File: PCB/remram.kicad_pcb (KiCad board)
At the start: 4 copper layers, 140 x 103 mm, 208 parts, among them J1 4DB-P108-06, J10 70543-0002, J11 Conn_02x13_Odd_Even, J12 70543-0002, J13 70543-0002, J14 70543-0002, J15 70543-0003, J16 62201021121, J17 70543-0001, J18 70543-0001, J19 70543-0001, J2 039531-1002, J20 70543-0003, J21 70543-0003, J22 70543-0003, J23 70543-0003, J3 70543-0002, J4 70543-0002, J5 70543-0002, J6 67068-8000, J7 Conn_02x05, J8 Conn_02x05, J9 70543-0002, Q1 PSMN1R2-30YLC,115, Q2 BUK9840-55, Q3 PSMN1R2-30YLC,115, Q4 BUK9840-55, SW1 OS102011MA1QN1, SW2 PTS645VL39-2, U1 TPS54308, U2 AP2112K-3.3TRG1, U3 ADUM4160, U4 STM32F765VIT6, U5 TMC2130-TA, U6 TMC2130-TA, U7 TMC2130-TA, U8 TMC2130-TA, Y1 TSX-3225 24.0000MF15X-AC3

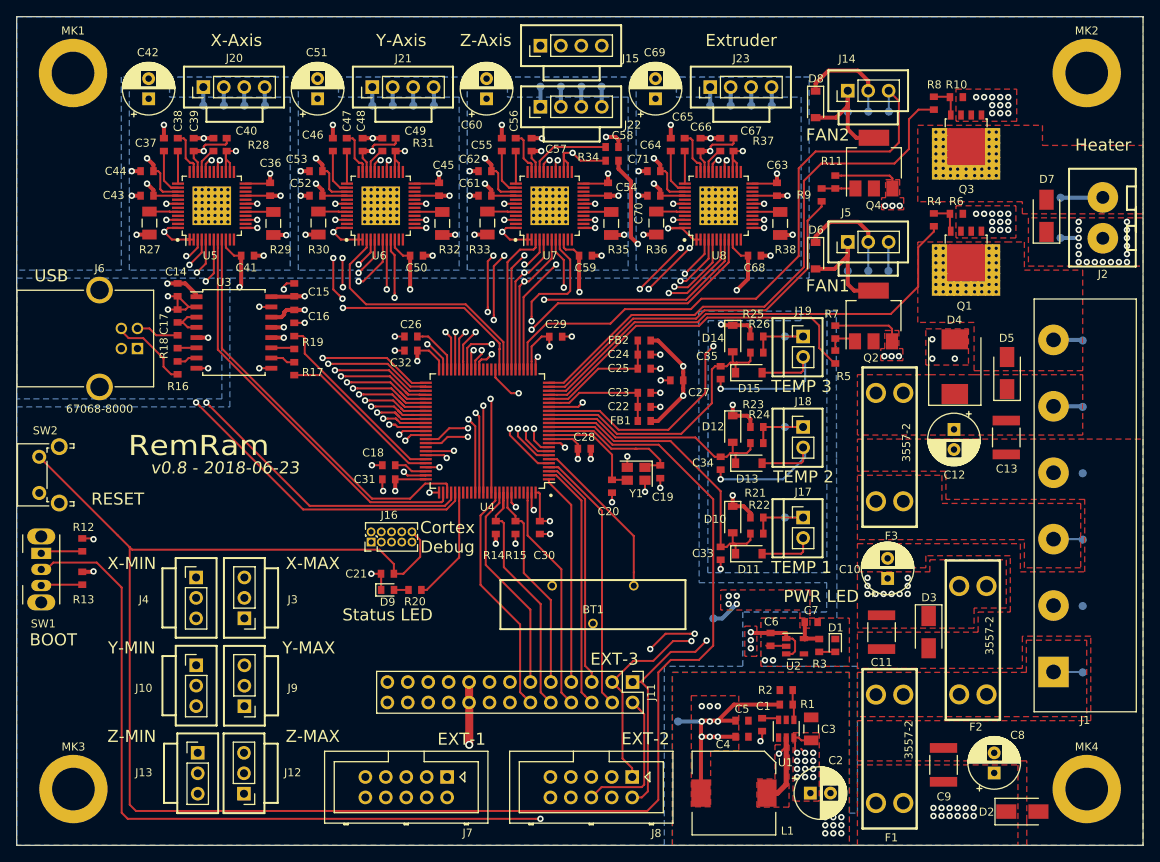
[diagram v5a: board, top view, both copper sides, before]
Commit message: Change DC-DC layout
The ripple on the 5V and 3V3 rail was too high (360mV).

In an attempt to reduce the RF and HF noise, I changed the layout
to a more compact one. I also added a third 22uF output capacitor
behind the inductor to lower ESR. I also added a 100nf input
capacitor to combat HF noise, as recommended in the datasheet.

The BOM needs to be updated in such a way, that we specificly
choose low ESR resistors.
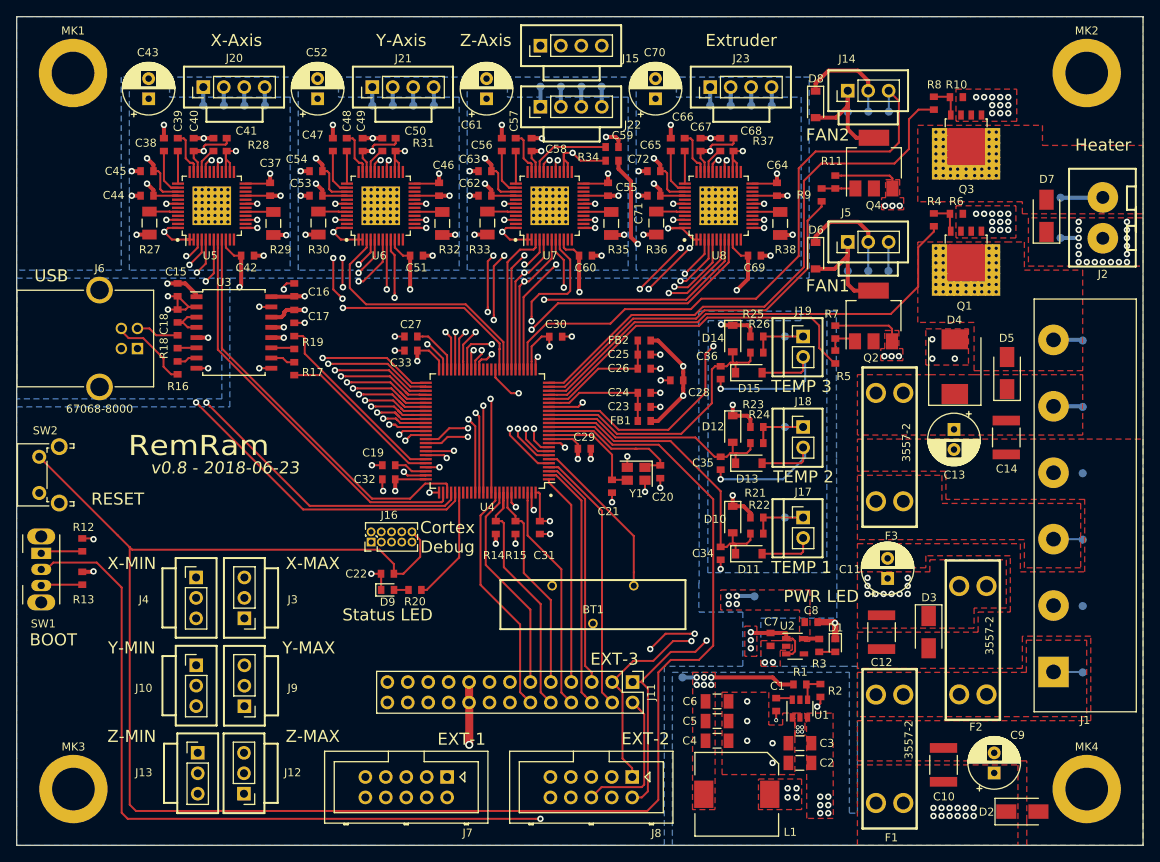
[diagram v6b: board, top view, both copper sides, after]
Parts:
- added C6: 22uF, Capacitor_SMD:C_1206_3216Metric, F.Cu at (149.2, 126.7)
- C2: value 100uF -> 10uF; footprint Capacitor_THT:CP_Radial_D6.3mm_P2.50mm -> Capacitor_SMD:C_1206_3216Metric
- C3: value 10uF -> 100nF
- C4, C5: footprint Capacitor_SMD:C_0603_1608Metric -> Capacitor_SMD:C_1206_3216Metric
- moved TP2 5.79 mm to (153.9, 113.6)
- moved TP1 5.50 mm to (144.9, 123.7)
- moved R2 4.25 mm to (162.1, 125.3), turned to 270 degrees
- moved C2 3.97 mm to (159.6, 134.3), turned to 180 degrees
- moved C4 3.14 mm to (149.2, 131.6)
- moved C5 3.10 mm to (149.2, 129.1)
- moved C1 3.05 mm to (156.6, 127.0)
- moved U1 3.02 mm to (159.6, 127.5)
- moved R1 3.02 mm to (159.6, 124.5)
- moved C3 2.26 mm to (159.6, 131.8), turned to 180 degrees
- moved L1 0.38 mm to (151.7, 138.2)
- renumbered C9 to C10, C10 to C11, C11 to C12, C12 to C13, C13 to C14, C14 to C15, C15 to C16, C16 to C17, C17 to C18, C18 to C19, C19 to C20, C20 to C21, C21 to C22, C22 to C23, C23 to C24, C24 to C25, C25 to C26, C26 to C27, C27 to C28, C28 to C29, C29 to C30, C30 to C31, C31 to C32, C32 to C33, C33 to C34, C34 to C35, C35 to C36, C36 to C37, C37 to C38, C38 to C39, C39 to C40, C40 to C41, C41 to C42, C42 to C43, C43 to C44, C44 to C45, C45 to C46, C46 to C47, C47 to C48, C48 to C49, C49 to C50, C50 to C51, C51 to C52, C52 to C53, C53 to C54, C54 to C55, C55 to C56, C56 to C57, C57 to C58, C58 to C59, C59 to C60, C60 to C61, C61 to C62, C62 to C63, C63 to C64, C64 to C65, C65 to C66, C66 to C67, C67 to C68, C68 to C69, C6 to C7, C69 to C70, C70 to C71, C71 to C72, C7 to C8, C8 to C9
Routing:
- net Net-(C1-Pad2): track 12.7 -> 1.50 mm, vias 2 -> 9
- net VDD5V: track 191.5 -> 182.1 mm, vias 17 -> 14
- net VDD3V3: track 111.6 -> 108.2 mm
- net GND: track 221.3 -> 224.7 mm, vias 114 -> 112
- net VDD_PWR: track 169.9 -> 173.1 mm, vias 41 -> 35

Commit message: Fix the SWD connector
I screwed up and switched the SWDIO and SWCLK pins.
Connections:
- J16 pad 2: /MCU/SWCLK -> /MCU/SWDIO
- J16 pad 4: /MCU/SWDIO -> /MCU/SWCLK
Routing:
- net /MCU/SWCLK: track 19.6 -> 9.67 mm
- net /MCU/SWDIO: track 12.7 -> 14.3 mm
